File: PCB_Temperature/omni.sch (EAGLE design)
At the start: 12 parts

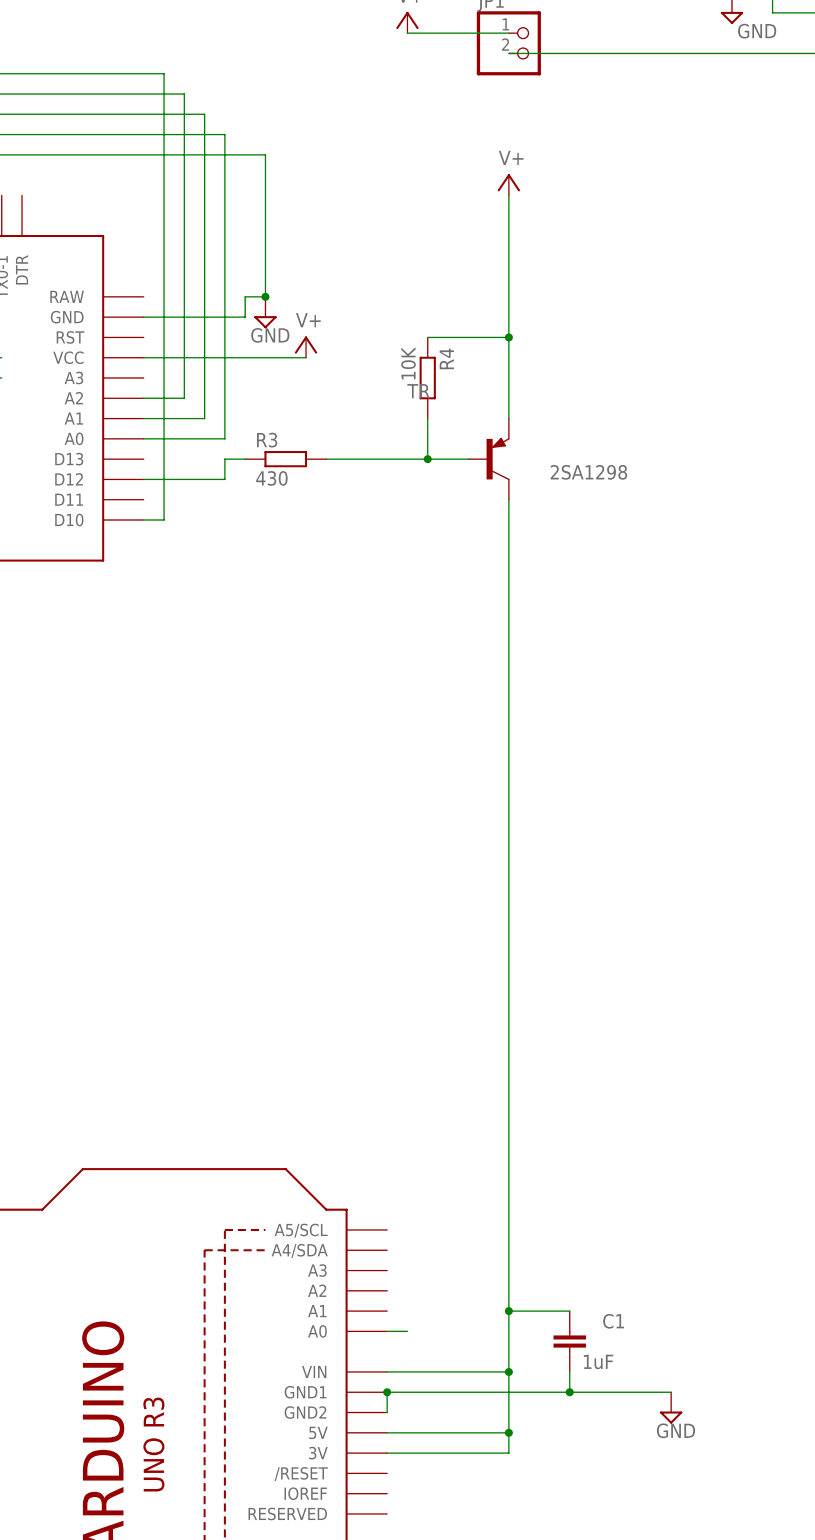
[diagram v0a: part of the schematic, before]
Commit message: Revise powersource for LoRa
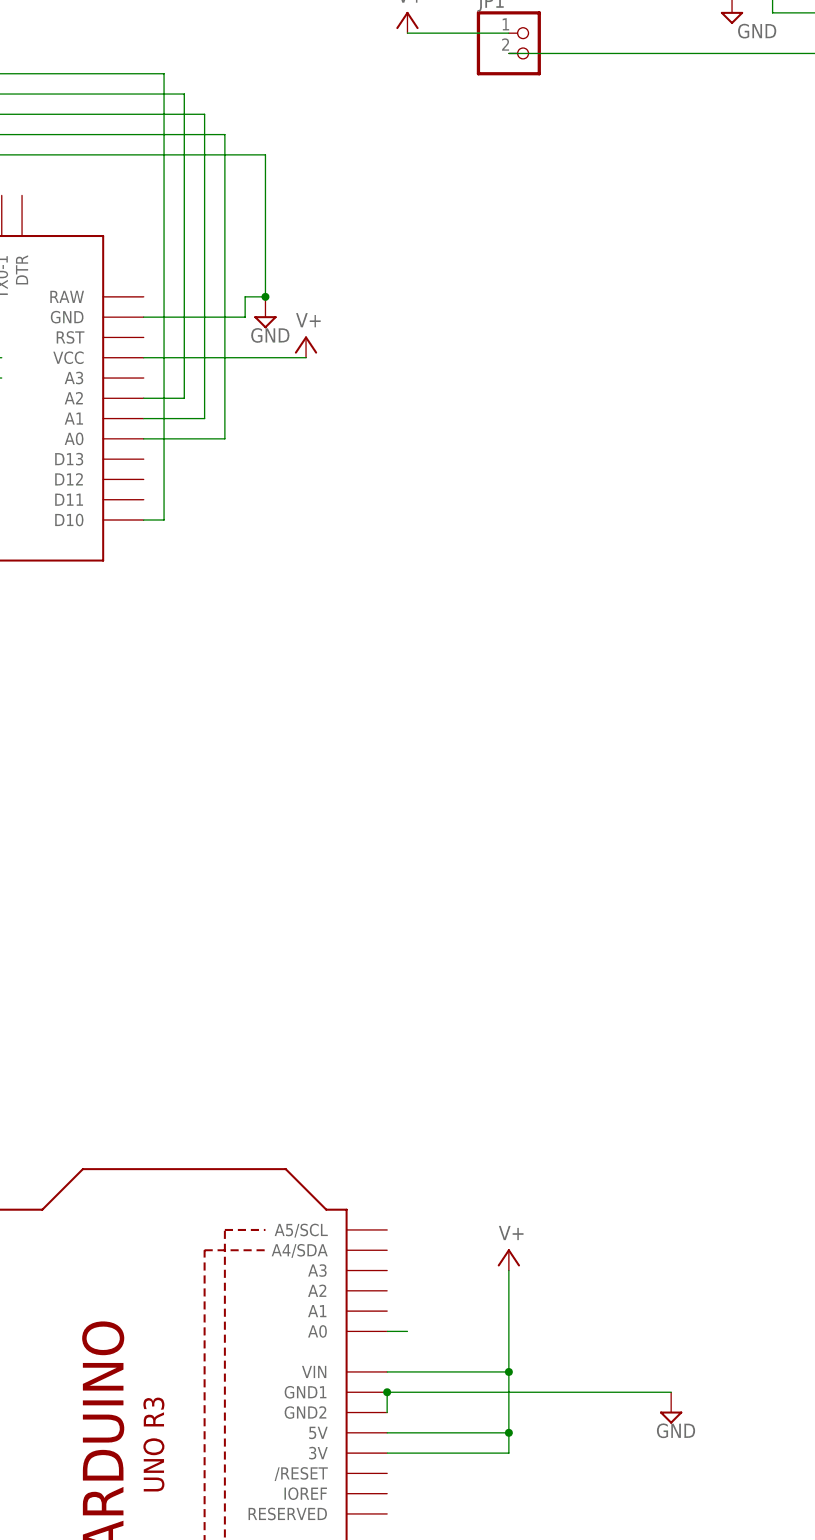
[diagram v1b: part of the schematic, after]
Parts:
- removed C1: 1uF, rcl:C-EUC2012
- removed R3: 430, rcl:R-EU_M2012
- removed R4: 10K, rcl:R-EU_M2012
- removed TR: 2SA1298, transistor-pnp:BF823SMD
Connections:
- removed net N$5: R3.1, U$1.D12
- removed net N$7: R3.2, R4.2, TR.B
- net GND: no longer C1.2
- net N$4: no longer C1.1, TR.C
- net V+: no longer R4.1, TR.E
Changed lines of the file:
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@@
 <parts>
 <part name="U$1" library="Arduino-clone" deviceset="PRO-MINI-2" device=""/>
-<part name="R3" library="rcl" library_urn="urn:adsk.eagle:library:334" deviceset="R-EU_" device="M2012" package3d_urn="urn:adsk.eagle:package:23561/1" value="430"/>
-<part name="R4" library="rcl" library_urn="urn:adsk.eagle:library:334" deviceset="R-EU_" device="M2012" package3d_urn="urn:adsk.eagle:package:23561/1" value="10K"/>
 <part name="LTE_LORA" library="adafruit" deviceset="ARDUINOR3" device="-BPLACE"/>
 <part name="JP1" library="pinhead" library_urn="urn:adsk.eagle:library:325" deviceset="PINHD-1X2" device="" package3d_urn="urn:adsk.eagle:package:22435/2"/>
-<part name="TR" library="transistor-pnp" library_urn="urn:adsk.eagle:library:399" deviceset="BF823*" device="SMD" package3d_urn="urn:adsk.eagle:package:29219/2" value="2SA1298"/>
 <part name="SUPPLY1" library="supply2" library_urn="urn:adsk.eagle:library:372" deviceset="GND" device=""/>
 <part name="SUPPLY4" library="supply2" library_urn="urn:adsk.eagle:library:372" deviceset="GND" device=""/>
@@
 <part name="SUPPLY14" library="supply2" library_urn="urn:adsk.eagle:library:372" deviceset="GND" device=""/>
 <part name="USB" library="OMNI" deviceset="MICROUSBCON" device="" value=""/>
-<part name="C1" library="rcl" library_urn="urn:adsk.eagle:library:334" deviceset="C-EU" device="C2012" package3d_urn="urn:adsk.eagle:package:23625/2" value="1uF"/>
 <part name="TEMP1" library="con-molex" library_urn="urn:adsk.eagle:library:165" deviceset="22-23-2031" device="" package3d_urn="urn:adsk.eagle:package:8078634/1"/>
 <part name="TEMP2" library="con-molex" library_urn="urn:adsk.eagle:library:165" deviceset="22-23-2031" device="" package3d_urn="urn:adsk.eagle:package:8078634/1"/>
@@
 <instances>
 <instance part="U$1" gate="G$1" x="40.64" y="66.04" smashed="yes"/>
-<instance part="R3" gate="G$1" x="78.74" y="58.42" smashed="yes">
-<attribute name="NAME" x="74.93" y="59.9186" size="1.778" layer="95"/>
-<attribute name="VALUE" x="74.93" y="55.118" size="1.778" layer="96"/>
-</instance>
-<instance part="R4" gate="G$1" x="96.52" y="68.58" smashed="yes" rot="R270">
-<attribute name="NAME" x="98.0186" y="72.39" size="1.778" layer="95" rot="R270"/>
-<attribute name="VALUE" x="93.218" y="72.39" size="1.778" layer="96" rot="R270"/>
-</instance>
 <instance part="LTE_LORA" gate="G$1" x="60.96" y="-60.96" smashed="yes" rot="R90"/>
 <instance part="JP1" gate="G$1" x="109.22" y="109.22" smashed="yes">
@@
 <attribute name="VALUE" x="102.87" y="104.14" size="1.778" layer="96"/>
 </instance>
-<instance part="TR" gate="G$1" x="104.14" y="58.42" smashed="yes">
-<attribute name="NAME" x="93.98" y="66.04" size="1.778" layer="95"/>
-<attribute name="VALUE" x="111.76" y="55.88" size="1.778" layer="96"/>
-</instance>
 <instance part="SUPPLY1" gate="GND" x="76.2" y="76.2" smashed="yes">
 <attribute name="VALUE" x="74.295" y="73.025" size="1.778" layer="96"/>
@@
 <attribute name="VALUE" x="92.71" y="115.57" size="1.778" layer="96"/>
 </instance>
-<instance part="SUPPLY8" gate="1" x="106.68" y="93.98" smashed="yes">
-<attribute name="VALUE" x="105.41" y="95.25" size="1.778" layer="96"/>
+<instance part="SUPPLY8" gate="1" x="106.68" y="-40.64" smashed="yes">
+<attribute name="VALUE" x="105.41" y="-39.37" size="1.778" layer="96"/>
 </instance>
 <instance part="SUPPLY9" gate="1" x="81.28" y="73.66" smashed="yes">
@@
 <attribute name="NAME" x="162.56" y="106.68" size="1.778" layer="95" rot="R180"/>
 <attribute name="VALUE" x="162.56" y="124.46" size="1.778" layer="96" rot="R180"/>
-</instance>
-<instance part="C1" gate="G$1" x="114.3" y="-50.8" smashed="yes">
-<attribute name="NAME" x="118.364" y="-50.419" size="1.778" layer="95"/>
-<attribute name="VALUE" x="115.824" y="-55.499" size="1.778" layer="96"/>
 </instance>
 <instance part="TEMP1" gate="-1" x="-15.24" y="96.52" smashed="yes" rot="R180">
@@
 <segment>
 <pinref part="LTE_LORA" gate="G$1" pin="3V"/>
-<pinref part="TR" gate="G$1" pin="C"/>
 <wire x1="106.68" y1="-66.04" x2="91.44" y2="-66.04" width="0.1524" layer="91"/>
-<wire x1="106.68" y1="53.34" x2="106.68" y2="-48.26" width="0.1524" layer="91"/>
 <pinref part="LTE_LORA" gate="G$1" pin="VIN"/>
-<wire x1="106.68" y1="-48.26" x2="106.68" y2="-55.88" width="0.1524" layer="91"/>
+<wire x1="106.68" y1="-43.18" x2="106.68" y2="-55.88" width="0.1524" layer="91"/>
 <wire x1="106.68" y1="-55.88" x2="91.44" y2="-55.88" width="0.1524" layer="91"/>
 <wire x1="106.68" y1="-55.88" x2="106.68" y2="-63.5" width="0.1524" layer="91"/>
@@
 <wire x1="106.68" y1="-66.04" x2="106.68" y2="-63.5" width="0.1524" layer="91"/>
 <junction x="106.68" y="-63.5"/>
-<pinref part="C1" gate="G$1" pin="1"/>
-<wire x1="114.3" y1="-48.26" x2="106.68" y2="-48.26" width="0.1524" layer="91"/>
-<junction x="106.68" y="-48.26"/>
-</segment>
-</net>
-<net name="N$7" class="0">
-<segment>
-<pinref part="R3" gate="G$1" pin="2"/>
-<wire x1="83.82" y1="58.42" x2="96.52" y2="58.42" width="0.1524" layer="91"/>
-<pinref part="TR" gate="G$1" pin="B"/>
-<pinref part="R4" gate="G$1" pin="2"/>
-<wire x1="96.52" y1="58.42" x2="101.6" y2="58.42" width="0.1524" layer="91"/>
-<wire x1="96.52" y1="63.5" x2="96.52" y2="58.42" width="0.1524" layer="91"/>
-<junction x="96.52" y="58.42"/>
+<pinref part="SUPPLY8" gate="1" pin="V+"/>
 </segment>
 </net>
@@
 <pinref part="SUPPLY5" gate="GND" pin="GND"/>
 <pinref part="LTE_LORA" gate="G$1" pin="GND1"/>
-<wire x1="127" y1="-58.42" x2="114.3" y2="-58.42" width="0.1524" layer="91"/>
 <pinref part="LTE_LORA" gate="G$1" pin="GND2"/>
-<wire x1="114.3" y1="-58.42" x2="91.44" y2="-58.42" width="0.1524" layer="91"/>
+<wire x1="127" y1="-58.42" x2="91.44" y2="-58.42" width="0.1524" layer="91"/>
 <wire x1="91.44" y1="-58.42" x2="91.44" y2="-60.96" width="0.1524" layer="91"/>
 <junction x="91.44" y="-58.42"/>
-<pinref part="C1" gate="G$1" pin="2"/>
-<wire x1="114.3" y1="-55.88" x2="114.3" y2="-58.42" width="0.1524" layer="91"/>
-<junction x="114.3" y="-58.42"/>
 </segment>
 <segment>
@@
 <pinref part="SUPPLY7" gate="1" pin="V+"/>
 </segment>
-<segment>
-<pinref part="SUPPLY8" gate="1" pin="V+"/>
-<pinref part="TR" gate="G$1" pin="E"/>
-<wire x1="106.68" y1="91.44" x2="106.68" y2="73.66" width="0.1524" layer="91"/>
-<pinref part="R4" gate="G$1" pin="1"/>
-<wire x1="106.68" y1="73.66" x2="106.68" y2="63.5" width="0.1524" layer="91"/>
-<wire x1="106.68" y1="73.66" x2="96.52" y2="73.66" width="0.1524" layer="91"/>
-<junction x="106.68" y="73.66"/>
-</segment>
 </net>
 <net name="N$1" class="0">
@@
 <pinref part="U$1" gate="G$1" pin="D8"/>
 <wire x1="-27.94" y1="53.34" x2="17.78" y2="53.34" width="0.1524" layer="91"/>
-</segment>
-</net>
-<net name="N$5" class="0">
-<segment>
-<pinref part="R3" gate="G$1" pin="1"/>
-<wire x1="73.66" y1="58.42" x2="71.12" y2="58.42" width="0.1524" layer="91"/>
-<wire x1="71.12" y1="58.42" x2="71.12" y2="55.88" width="0.1524" layer="91"/>
-<pinref part="U$1" gate="G$1" pin="D12"/>
-<wire x1="71.12" y1="55.88" x2="60.96" y2="55.88" width="0.1524" layer="91"/>
 </segment>
 </net>
@@
 packages will not be understood (or retained) with this version.
 </note>
-<note version="8.4" severity="warning">
-Since Version 8.4, EAGLE supports properties for SPICE simulation.
-Probes in schematics and SPICE mapping objects found in parts and library devices
-will not be understood with this version. Update EAGLE to the latest version
-for full support of SPICE simulation.
-</note>
 </compatibility>
